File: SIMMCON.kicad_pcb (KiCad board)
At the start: 2 copper layers, 12 parts, among them J1 Conn_02x12_Odd_Even, J2 Conn_02x13_Odd_Even, U0 PALCE16V8H, U1 74AC(T)245, U2 74AC(T)245

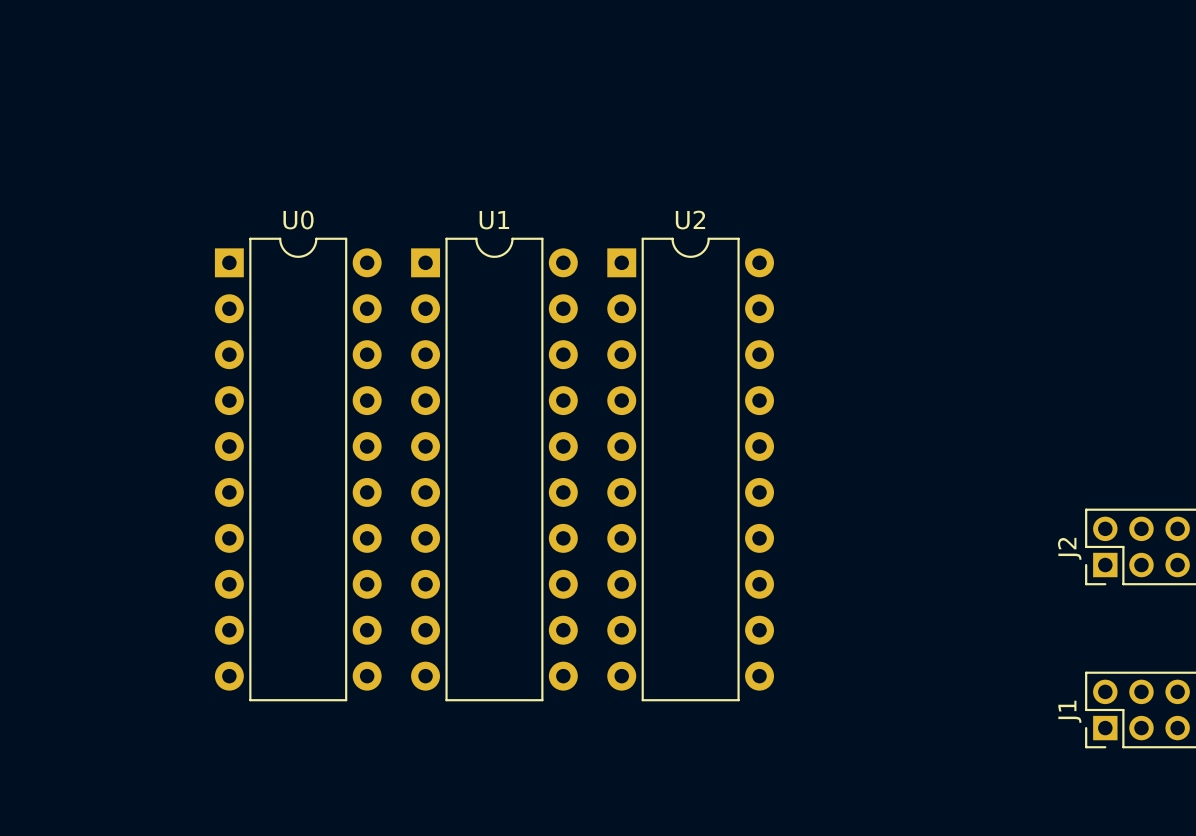
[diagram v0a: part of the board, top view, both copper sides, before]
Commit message: update some parts to soic
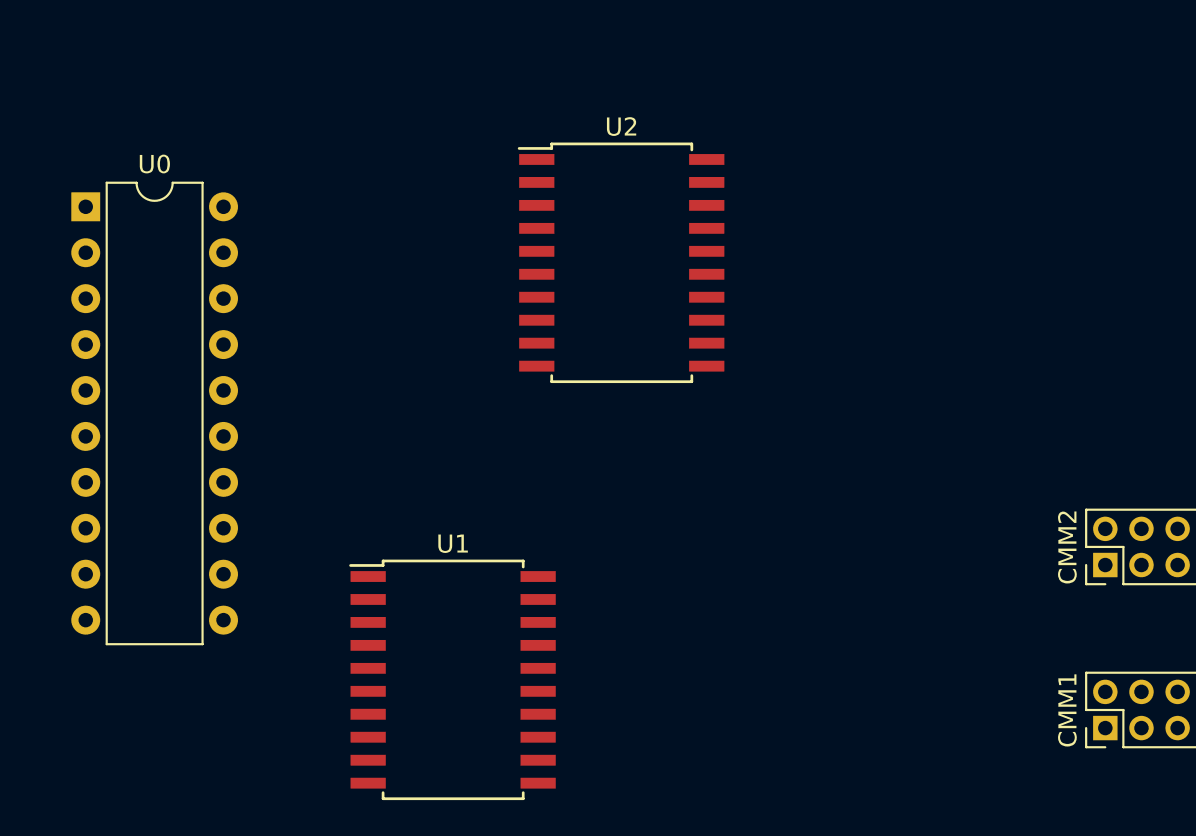
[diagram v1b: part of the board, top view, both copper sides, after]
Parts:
- U1, U2: footprint Housings_DIP:DIP-20_W7.62mm -> Housings_SOIC:SOIC-20W_7.5x12.8mm_Pitch1.27mm
- moved U1 23.1 mm to (95.1, 93.9)
- moved U0 8.53 mm to (74.8, 67.7)
- renumbered J1 to CMM1, J2 to CMM2

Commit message: updates
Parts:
- C2, C3, C4: footprint Capacitors_THT:C_Axial_L3.8mm_D2.6mm_P7.50mm_Horizontal -> Capacitors_SMD:C_0805
- R1: footprint Resistors_THT:R_Axial_DIN0204_L3.6mm_D1.6mm_P1.90mm_Vertical -> Resistors_SMD:R_0805
- U0: footprint Housings_DIP:DIP-20_W7.62mm -> Housings_LCC:PLCC-20_SMD-Socket
- moved C2 128.7 mm to (51.2, 117.1), turned to 270 degrees
- moved C4 123.2 mm to (67.7, 118.1), turned to 270 degrees
- moved JP2 100.3 mm to (100.7, 132.8), turned to 90 degrees
- moved JP1 97.9 mm to (100.6, 136.7), turned to 90 degrees
- moved R1 95.9 mm to (82.9, 116.8), turned to 270 degrees
- moved U0 70.6 mm to (116.8, 124.5)
- moved SIMM72 67.0 mm to (99.1, 110.5)
- moved U2 54.5 mm to (95.2, 124.5), turned to 180 degrees
- moved U1 52.0 mm to (137.2, 124.5), turned to 180 degrees
- moved C3 44.8 mm to (153.2, 130.6), turned to 90 degrees
- moved J2 40.3 mm to (131.2, 136.8)
- moved J1 12.8 mm to (131.2, 100.3)
- renumbered CMM2 to J1, CMM1 to J2, SIMM1 to SIMM72
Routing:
- net D15: track 0.00 -> 101.8 mm
- net D14: track 0.00 -> 98.6 mm
- net D13: track 0.00 -> 92.4 mm
- net D12: track 0.00 -> 91.2 mm
- net D11: track 0.00 -> 84.9 mm
- net D10: track 0.00 -> 83.7 mm
- net D9: track 0.00 -> 77.1 mm
- net D8: track 0.00 -> 76.4 mm
- net WE: track 0.00 -> 75.5 mm, vias 0 -> 2
- net D4: track 0.00 -> 68.9 mm
- net A7: track 0.00 -> 63.7 mm, vias 0 -> 1
- net A9: track 0.00 -> 59.5 mm, vias 0 -> 2
- net A8: track 0.00 -> 57.4 mm, vias 0 -> 2
- net BASEM1: track 0.00 -> 54.9 mm, vias 0 -> 1
- net A10: track 0.00 -> 53.4 mm
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- added copper zone on B.Cu, net GND
- added copper zone on F.Cu, net VCC
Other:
- board outline added: 119.4 x 44.4 mm
- copper layers 2 -> 4
- board text added: "NOT YET READY"

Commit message: updates
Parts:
- moved U2 19.1 mm to (76.2, 123.2)
- moved U0 14.0 mm to (102.9, 123.2), turned to 90 degrees
- moved U1 7.73 mm to (129.5, 123.2)
- moved JP2 6.38 mm to (105.4, 137.2)
- moved JP1 5.11 mm to (95.5, 137.2)
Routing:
- net VCC: track 0.00 -> 322.2 mm, vias 0 -> 4
- net GND: track 21.4 -> 268.0 mm, vias 7 -> 6
- net A8: track 57.4 -> 90.8 mm, vias 2 -> 1
- net A9: track 59.5 -> 89.1 mm
- net AB9: track 22.8 -> 46.3 mm, vias 0 -> 1
- net A6: track 24.5 -> 46.8 mm, vias 1 -> 3
- net AB8: track 23.6 -> 44.5 mm, vias 0 -> 1
- net AB10: track 45.4 -> 66.2 mm, vias 1 -> 2
- net D11: track 84.9 -> 105.5 mm, vias 0 -> 1
- net A10: track 53.4 -> 73.8 mm, vias 0 -> 3
- net CAS: track 43.5 -> 63.8 mm, vias 1 -> 3
- net D4: track 68.9 -> 51.9 mm
- net A11: track 51.1 -> 68.1 mm
- net AB11: track 29.5 -> 45.7 mm, vias 1 -> 2
- net RAS: track 33.6 -> 47.4 mm, vias 1 -> 0
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- added copper zone on F.Cu, net GND
- removed copper zone on F.Cu, net VCC
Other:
- copper layers 4 -> 2
- board text added: "FRONT TOWARD ENEMY"
- board text removed: "NOT YET READY"

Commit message: updates
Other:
- board text added: "NOT YET READY - DO NOT USE"
